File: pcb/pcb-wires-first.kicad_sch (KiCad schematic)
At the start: 1 part, among them U1 SLG47115V

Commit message: Drafting.
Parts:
- added C2, C3: 100nF, Capacitor_SMD:C_0603_1608Metric, symbol Device:C
- added D1: ON, Diode_SMD:D_0603_1608Metric, symbol Device:LED
- added D2: FAULT, Diode_SMD:D_0603_1608Metric, symbol Device:LED
- added J1: Conn_01x06, symbol Connector_Generic:Conn_01x06
- added J2: Conn_01x02, symbol Connector_Generic:Conn_01x02
- added J3: Conn_01x04, Connector_PinHeader_2.54mm:PinHeader_1x04_P2.54mm_Vertical, symbol Connector_Generic:Conn_01x04
- added J4: Conn_01x06, Connector_PinHeader_2.54mm:PinHeader_1x06_P2.54mm_Vertical, symbol Connector_Generic:Conn_01x06
- added R1, R2: 510, Resistor_SMD:R_0603_1608Metric, symbol Device:R
- added SW1, SW2: SW_Push, Button_Switch_SMD:SW_SPST_B3U-1000P, symbol Switch:SW_Push
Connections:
- net VDD: now reaches U1.1 (V_{DD})
- net VDD: now also C3.2, J2.1 (Pin_1)
- net at U1.10 (HV_GPO1): now also U1.9 (HV_GPO1), J3.3 (Pin_3)
- net VDD2: now reaches U1.11 (V_{DD2})
- net VDD2: now also U1.6 (V_{DD2}), C2.2, J3.4 (Pin_4)
- net HV_GND: now reaches U1.13 (HV_GND)
- net HV_GND: now also U1.4 (HV_GND), C2.1, J3.1 (Pin_1)
- net at U1.14 (GPIO1): now also J4.2 (Pin_2), R2.1
- net at U1.15 (SCL): now also J4.5 (Pin_5)
- net at U1.16 (SDA): now also J4.4 (Pin_4)
- net at U1.17 (GPIO4): now also J4.3 (Pin_3), R1.1
- net GND: now reaches U1.18 (GND)
- net GND: now also C3.1, D1.1 (K), D2.1 (K), J2.2 (Pin_2), SW1.1, SW2.1
- net turn-on-hw: now reaches U1.19 (GPIO5)
- net turn-off-sw: now reaches U1.2 (GPIO0)
- net turn-off-sw: now also SW1.2
- net turn-on-sw: now reaches U1.20 (GPIO6)
- net turn-on-sw: now also SW2.2
- net turn-off-hw: now reaches U1.3 (GPI)
- net at U1.7 (HV_GPO0): now also U1.8 (HV_GPO0), J3.2 (Pin_2)
- new net: D1.2 (A), R1.2
- new net: D2.2 (A), R2.2
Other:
- moved on the sheet: U1

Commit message: Drafting the board.
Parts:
- removed J1: Conn_01x06, symbol Connector_Generic:Conn_01x06
- removed J3: Conn_01x04, Connector_PinHeader_2.54mm:PinHeader_1x04_P2.54mm_Vertical, symbol Connector_Generic:Conn_01x04
- removed J4: Conn_01x06, Connector_PinHeader_2.54mm:PinHeader_1x06_P2.54mm_Vertical, symbol Connector_Generic:Conn_01x06
- added A1: Arduino_Nano_ESP32, Module:Arduino_Nano, symbol MCU_Module:Arduino_Nano_ESP32
- added C10, C11, C12, C13, C14, C15, C16, C4, C5, C6, C7, C8, C9: 100nF, Capacitor_SMD:C_0603_1608Metric, symbol Device:C
- added D3, D4: ON, Diode_SMD:D_0603_1608Metric, symbol Device:LED
- added J10, J11, J9: Conn_01x02, Connector_Phoenix_MC:PhoenixContact_MCV_1,5_2-G-3.5_1x02_P3.50mm_Vertical, symbol Connector_Generic:Conn_01x02
- added J5, J6, J7: Conn_01x04, Connector_Phoenix_MC:PhoenixContact_MCV_1,5_4-G-3.5_1x04_P3.50mm_Vertical, symbol Connector_Generic:Conn_01x04
- added R3, R4: 510, Resistor_SMD:R_0603_1608Metric, symbol Device:R
- added SW3: on-1, Button_Switch_SMD:SW_SPST_B3U-1000P, symbol Switch:SW_Push
- added SW4: off-1, Button_Switch_SMD:SW_SPST_B3U-1000P, symbol Switch:SW_Push
- added SW5: on-3, Button_Switch_SMD:SW_SPST_B3U-1000P, symbol Switch:SW_Push
- added SW6: off-3, Button_Switch_SMD:SW_SPST_B3U-1000P, symbol Switch:SW_Push
- added U2: SLG46826V, Package_DFN_QFN:Renesas_UQFN-20_2x3mm_P0.4mm_LayoutBorder4x6y, symbol local-lib:SLG46826V
- added U3: R-78C3.3-1.0, Converter_DCDC:Converter_DCDC_RECOM_R-78E-0.5_THT, symbol Converter_DCDC:R-78C3.3-1.0
- J2: footprint (none) -> Connector_Phoenix_MSTB:PhoenixContact_MSTBVA_2,5_2-G-5,08_1x02_P5.08mm_Vertical
- SW1: value SW_Push -> off-2
- SW2: value SW_Push -> on-2
- U1: symbol local-lib:SLG47115V -> local-lib:SLG47105V
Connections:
- net HV_GND is gone; now on net GND: C2.1, U1.13 (HV_GND), U1.4 (HV_GND)
- net GND: now also J2.1 (Pin_1), SW1.2, SW2.2, C10.1, C11.1, C12.1, C13.1, C14.1, C15.1, C16.1, C4.1, C5.1, C6.1, C7.1, C8.1, C9.1, D3.1 (K), D4.1 (K), J10.1 (Pin_1), J11.1 (Pin_1), J9.1 (Pin_1), SW3.2, SW4.2, SW5.2, SW6.2, U2.11 (GND), U3.2 (GND); no longer D2.1 (K), J2.2 (Pin_2), SW1.1, SW2.1
- net VDD: now also A1.30 (VIN), C16.2, U2.1 (V_{DD}), U3.3 (OUT); no longer J2.1 (Pin_1)
- net VDD2: now also J2.2 (Pin_2), U3.1 (IN)
- net at U1.17 (GPIO4): now also A1.19 (A0), R4.1, U2.16 (IO10); no longer R1.1
- net at U1.14 (GPIO1): now also A1.20 (A1), R3.1, U2.15 (IO9); no longer R2.1
- net at U1.7 (HV_GPO0): now also J11.2 (Pin_2); no longer U1.8 (HV_GPO0)
- net at U1.9 (HV_GPO2): now also J9.2 (Pin_2); no longer U1.10 (HV_GPO1)
- net turn-off-hw: no longer names the net of U1.3 (GPI)
- net turn-off-sw: no longer names the net of U1.2 (GPIO0)
- net turn-off-sw: now also R1.1, A1.21 (A2), U2.13 (IO8); no longer SW1.2
- net turn-on-hw: no longer names the net of U1.19 (GPIO5)
- net turn-on-sw: no longer names the net of U1.20 (GPIO6)
- net turn-on-sw: no longer SW2.2
- new net: A1.29 (GND), A1.4 (GND)
- new net: D3.2 (A), R3.2
- new net: D4.2 (A), R4.2
- new net: J10.2 (Pin_2), U1.8 (HV_GPO1)
- new net off-1a: C9.2, J5.3 (Pin_3), SW4.1, U2.4 (IO2)
- new net off-1b: A1.1 (D1/TX), C8.2, J5.4 (Pin_4), U2.5 (IO3)
- new net off-2a: C6.2, J6.3 (Pin_3), SW1.1, U2.10 (IO6)
- new net off-2b: A1.6 (D3), C4.2, J6.4 (Pin_4), U2.12 (IO7)
- new net off-3a: C14.2, J7.3 (Pin_3), SW6.1, U2.19 (IO13)
- new net off-3b: A1.8 (D5), C15.2, J7.4 (Pin_4), U2.20 (IO14)
- new net on-1a: C11.2, J5.1 (Pin_1), SW3.1, U2.2 (IO0)
- new net on-1b: A1.2 (D0/RX), C10.2, J5.2 (Pin_2), U2.3 (IO1)
- new net on-2a: C7.2, J6.1 (Pin_1), SW2.1, U2.6 (IO4)
- new net on-2b: A1.5 (D2), C5.2, J6.2 (Pin_2), U2.7 (IO5)
- new net on-3a: C12.2, J7.1 (Pin_1), SW5.1, U2.17 (IO11)
- new net on-3b: A1.7 (D4), C13.2, J7.2 (Pin_2), U2.18 (IO12)
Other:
- note added: "Debounce capacitors (all 100nF)"
- moved on the sheet: C2, C3, D1, D2, J2, R1, R2, SW1, SW2, U1

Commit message: WIP.
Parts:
- removed D2: FAULT, Diode_SMD:D_0603_1608Metric, symbol Device:LED
- removed R2: 510, Resistor_SMD:R_0603_1608Metric, symbol Device:R
- added D5: FAULT, Diode_SMD:D_0603_1608Metric, symbol Device:LED
- added H1, H2, H3, H4: MountingHole, MountingHole:MountingHole_3.2mm_M3, symbol Mechanical:MountingHole
- added NT1, NT2: NetTie_2, symbol Device:NetTie_2
- added R5: 510, Resistor_SMD:R_0603_1608Metric, symbol Device:R
- J10, J11, J9: footprint Connector_Phoenix_MC:PhoenixContact_MCV_1,5_2-G-3.5_1x02_P3.50mm_Vertical -> Connector_JST:JST_VH_B2P-VH-FB-B_1x02_P3.96mm_Vertical
- J2: footprint Connector_Phoenix_MSTB:PhoenixContact_MSTBVA_2,5_2-G-5,08_1x02_P5.08mm_Vertical -> Connector_JST:JST_VH_B2P-VH-FB-B_1x02_P3.96mm_Vertical
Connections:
- net GND: now also A1.29 (GND), A1.4 (GND), D5.1 (K), NT1.2; no longer C2.1, J10.1 (Pin_1), J11.1 (Pin_1), J2.1 (Pin_1), J9.1 (Pin_1), U1.13 (HV_GND), U1.4 (HV_GND)
- net VDD: now also NT2.1
- net at U1.19 (GPIO5): now also R5.1
- net at U2.14 (V_{DD2}): now also NT2.2
- new net: D5.2 (A), R5.2
- new net HV_GND: C2.1, J10.1 (Pin_1), J11.1 (Pin_1), J2.1 (Pin_1), J9.1 (Pin_1), NT1.1, U1.13 (HV_GND), U1.4 (HV_GND)
- no-connect marks 0 -> 20
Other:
- moved on the sheet: C2, C3, J10, J11, J9, U1

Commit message: Working on PSU part mostly.
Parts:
- added C1: 4.7μF/50V, Capacitor_SMD:C_1206_3216Metric, symbol Device:C
- added C17: 10μF/50V, Capacitor_SMD:C_1206_3216Metric, symbol Device:C
- added C18: 4.7μF/16V, Capacitor_SMD:C_0603_1608Metric, symbol Device:C
- added L1: 10μF/4A, Inductor_SMD:L_Bourns_SRP7028A_7.3x6.6mm, symbol Device:L
- NT1: value NetTie_2 -> gnd-bridge
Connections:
- net GND: now also C18.2
- net HV_GND: no longer J2.1 (Pin_1), NT1.1
- net VDD: now also A1.17 (3V3); no longer A1.30 (VIN), U3.3 (OUT)
- net VDD2: no longer J2.2 (Pin_2), U3.1 (IN)
- new net 3V3: C18.1, U3.3 (OUT)
- new net HV-GND: C1.2, C17.2, J2.1 (Pin_1), NT1.1
- new net HV-VDD: C1.1, L1.2, U3.1 (IN)
- new net hv-in-1: C17.1, J2.2 (Pin_2), L1.1
- no-connect marks 20 -> 22
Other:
- moved on the sheet: J2, U3

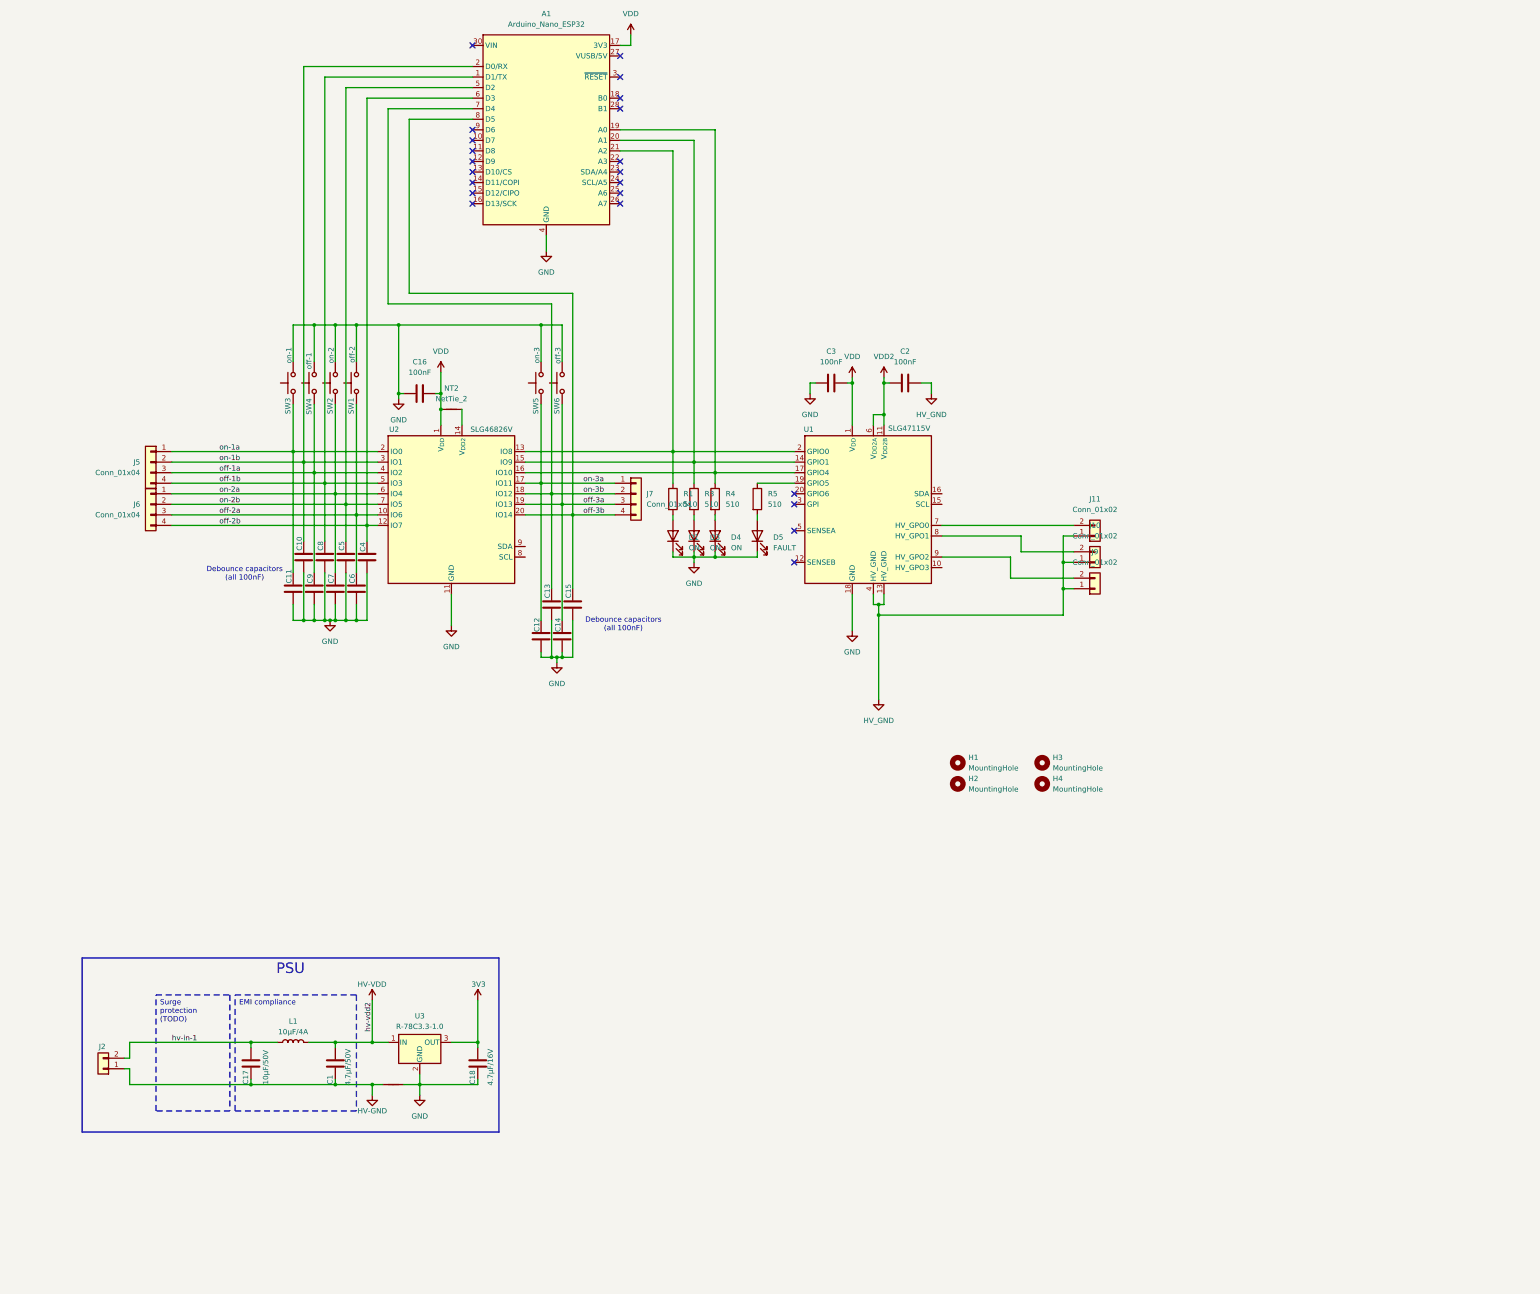
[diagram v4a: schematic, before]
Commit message: Getting rid of the warnings.
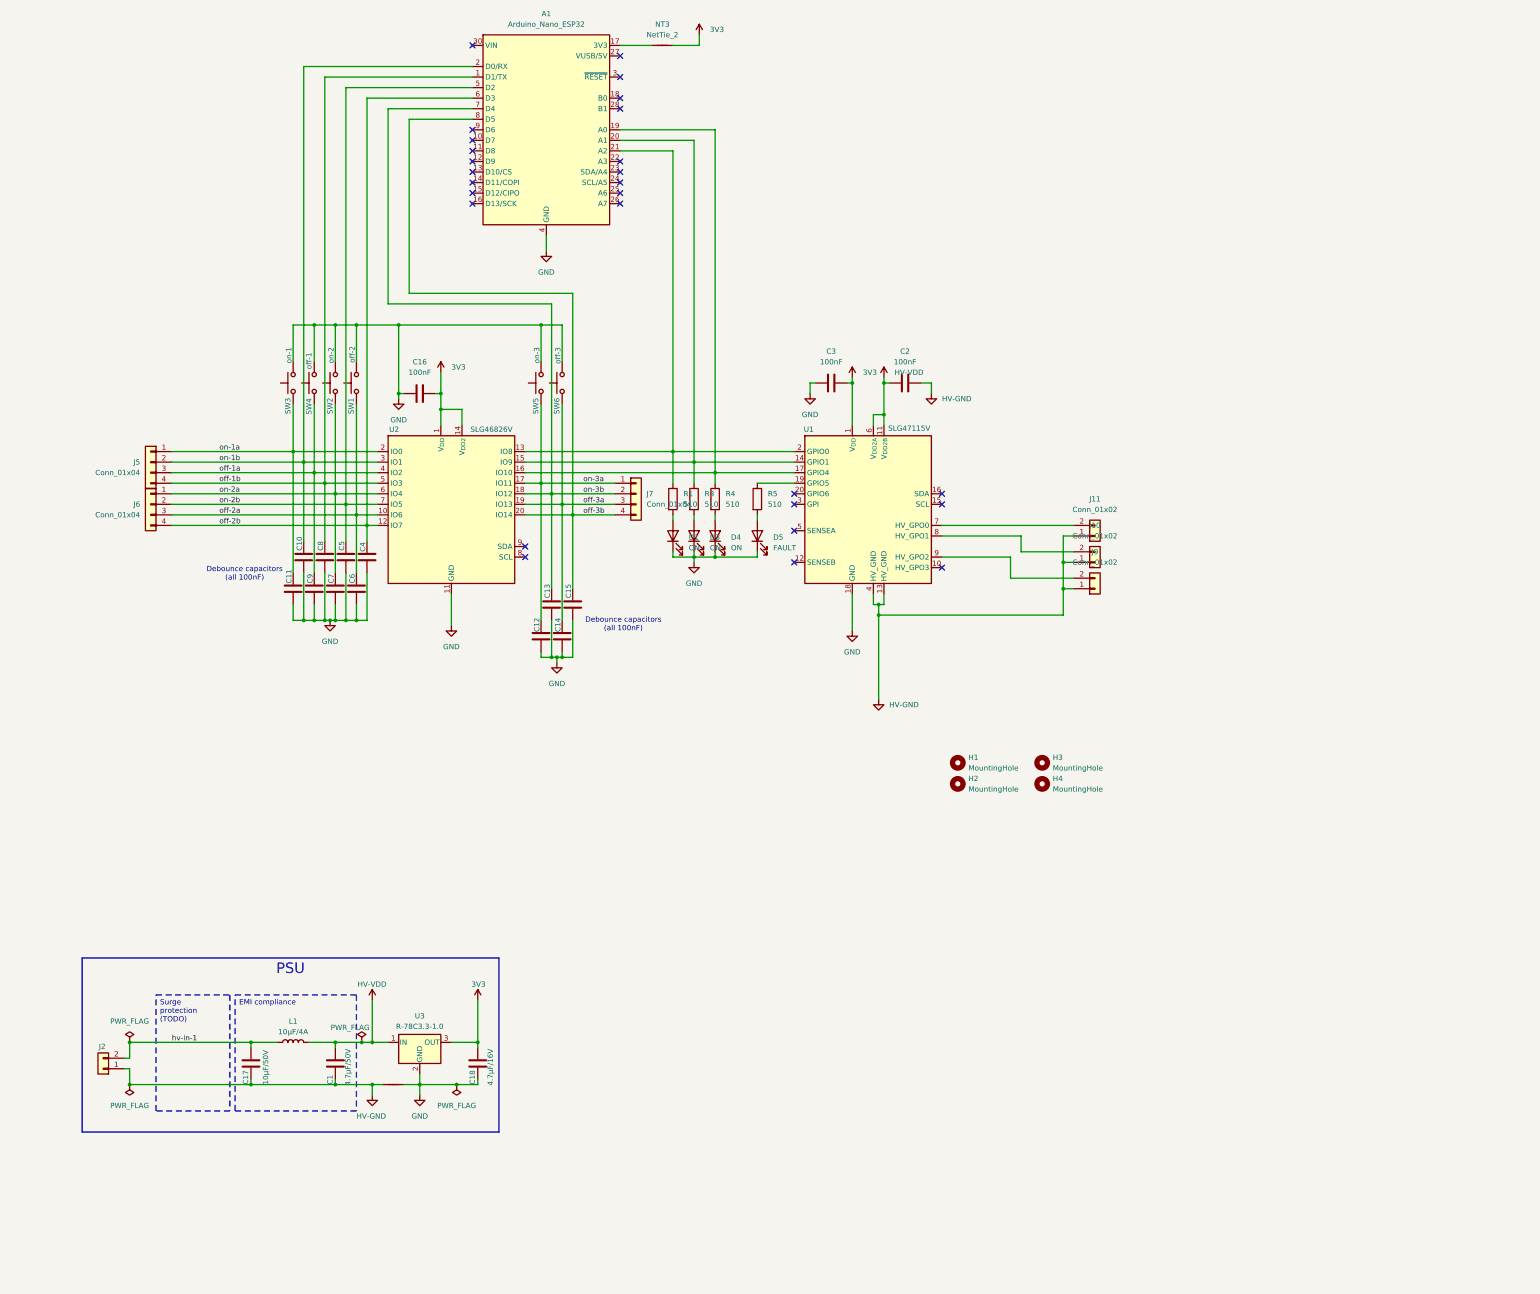
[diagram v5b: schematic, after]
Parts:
- removed NT2: NetTie_2, symbol Device:NetTie_2
- added NT3: NetTie_2, symbol Device:NetTie_2
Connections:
- net HV_GND is gone; now on net HV-GND: C2.1, J10.1 (Pin_1), J11.1 (Pin_1), J9.1 (Pin_1), U1.13 (HV_GND), U1.4 (HV_GND)
- net VDD2 is gone; now on net HV-VDD: C2.2, U1.11 (V_{DD2B}), U1.6 (V_{DD2A})
- net 3V3: now also C16.2, C3.2, U1.1 (V_{DD}), U2.1 (V_{DD}), U2.14 (V_{DD2}), NT3.2
- removed net VDD: A1.17 (3V3), C16.2, C3.2, U1.1 (V_{DD}), U2.1 (V_{DD})
- new net: A1.17 (3V3), NT3.1
- no-connect marks 22 -> 27

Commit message: WIP.
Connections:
- net switch-1: now reaches A1.21 (A2), R1.1, U1.2 (GPIO0), U2.13 (IO8)
- net output-1: now reaches J11.2 (Pin_2), U1.7 (HV_GPO0)
- net output-3: now reaches J9.2 (Pin_2), U1.9 (HV_GPO2)
- net output-2: now reaches J10.2 (Pin_2), U1.8 (HV_GPO1)
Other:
- moved on the sheet: A1, C1, C10, C11, C12, C13, C14, C15, C16, C17, C18, C2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

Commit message: Tidying up schematic.
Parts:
- removed D3, D4: ON, Diode_SMD:D_0603_1608Metric, symbol Device:LED
- removed D5: FAULT, Diode_SMD:D_0603_1608Metric, symbol Device:LED
- removed R3, R4, R5: 510, Resistor_SMD:R_0603_1608Metric, symbol Device:R
- added D2: ON2, Diode_SMD:D_0603_1608Metric, symbol Device:LED
- added D6: ON3, Diode_SMD:D_0603_1608Metric, symbol Device:LED
- added D7: FAULT, Diode_SMD:D_0603_1608Metric, symbol Device:LED
- added R2, R6, R7: 2.2k, Resistor_SMD:R_0603_1608Metric, symbol Device:R
- D1: value ON -> ON1
- R1: value 510 -> 2.2k
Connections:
- net GND: now also D2.1 (K), D6.1 (K), D7.1 (K)
- net fault: now reaches U1.19 (GPIO5)
- net fault: now also A1.22 (A3)
- net switch-3: now reaches A1.19 (A0), U1.17 (GPIO4), U2.16 (IO10)
- net switch-3: now also R6.1, R7.1
- net switch-2: now reaches A1.20 (A1), U1.14 (GPIO1), U2.15 (IO9)
- net switch-2: now also R2.1
- new net: D7.2 (A), R7.2
- new net: D6.2 (A), R6.2
- new net: D2.2 (A), R2.2
- no-connect marks 27 -> 26
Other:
- moved on the sheet: A1, C1, C10, C11, C12, C13, C14, C15, C16, C17, C18, C2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

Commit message: Routing the board.
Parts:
- added D5: 3V3, Diode_SMD:D_0603_1608Metric, symbol Device:LED
- added D6: HV, Diode_SMD:D_0603_1608Metric, symbol Device:LED
- added R5: 2.2k, Resistor_SMD:R_0603_1608Metric, symbol Device:R
- added R6: 6.7k, Resistor_SMD:R_0603_1608Metric, symbol Device:R
- renumbered C11 to C1, C12 to C10, C13 to C11, C14 to C12, C15 to C13, C3 to C14, C17 to C15, C2 to C16, C1 to C17, C10 to C2, C9 to C3, C8 to C4, C7 to C5, C5 to C6, C6 to C7, C4 to C8, C16 to C9, D6 to D3, D7 to D4, J5 to J1, J6 to J2, J7 to J3, J2 to J4, J11 to J5, J10 to J6, J9 to J7, NT3 to NT1, NT1 to NT2, R6 to R3, R7 to R4, SW3 to SW1, SW4 to SW2, SW2 to SW3, SW1 to SW4, U2 to U1, U1 to U2
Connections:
- net 3V3: now also R5.1
- net GND: now also D5.1 (K), D6.1 (K)
- net HV-VDD: now also R6.1
- new net: D6.2 (A), R6.2
- new net: D5.2 (A), R5.2
